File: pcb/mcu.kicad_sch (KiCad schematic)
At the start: 0 parts

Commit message: [pcb] Started STM32 schematic
Co-authored-by: Siddhant Kameswar <grimsteel@users.noreply.github.com>
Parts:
- added C1, C4, C5, C6, C7: 100nF, symbol Device:C
- added C2, C3, C8: 10uF, symbol Device:C
- added D1: D, symbol Device:D
- added J1: Conn_01x02_Pin, symbol Connector:Conn_01x02_Pin
- added R1: 1K, symbol Device:R
- added U1: STM32H750VBTx, Package_QFP:LQFP-100_14x14mm_P0.5mm, symbol MCU_ST_STM32H7:STM32H750VBTx
- added U2: W25Q64JVSSIQ_C179171, lcsc:SOIC-8_L5.3-W5.3-P1.27-LS8.0-BL, symbol lcsc:W25Q64JVSSIQ_C179171
- added U3: AMS1117-3.3, Package_TO_SOT_SMD:SOT-223-3_TabPin2, symbol Regulator_Linear:AMS1117-3.3
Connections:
- new net: R1.1, U1.6 (VBAT)
- new net: D1.2 (A), J1.1 (Pin_1)
- new net: U1.10 (VSS), U1.26 (VSS), U1.49 (VSS), U1.74 (VSS), U1.99 (VSS)
- new net +3.3V: C1.2, C3.1, C4.1, C5.1, C6.1, C7.1, C8.1, R1.2, U1.100 (VDD), U1.11 (VDD), U1.27 (VDD), U1.50 (VDD), U1.75 (VDD), U2.8 (VCC), U3.2 (VO)
- new net +BATT: C2.2, D1.1 (K), U3.3 (VI)
- new net BOOT0: U1.94 (BOOT0)
- new net FLASH_CS: U1.92 (PB6), U2.1 (~{CS})
- new net FLASH_IO_0: U1.58 (PD11), U2.5 (DI(IO0))
- new net FLASH_IO_1: U1.59 (PD12), U2.2 (DO(IO1))
- new net FLASH_IO_2: U1.1 (PE2), U2.3 (WP#(IO2))
- new net FLASH_IO_3: U1.60 (PD13), U2.7 (HOLD#orRESET#(IO3))
- new net GND: C1.1, C2.1, C3.2, C4.2, C5.2, C6.2, C7.2, C8.2, J1.2 (Pin_2), U2.4 (GND), U3.1 (GND)
- new net SPI_CLK: U1.36 (PB2), U2.6 (CLK)
- no-connect marks 0 -> 1
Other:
- note added: "Battery Connector"

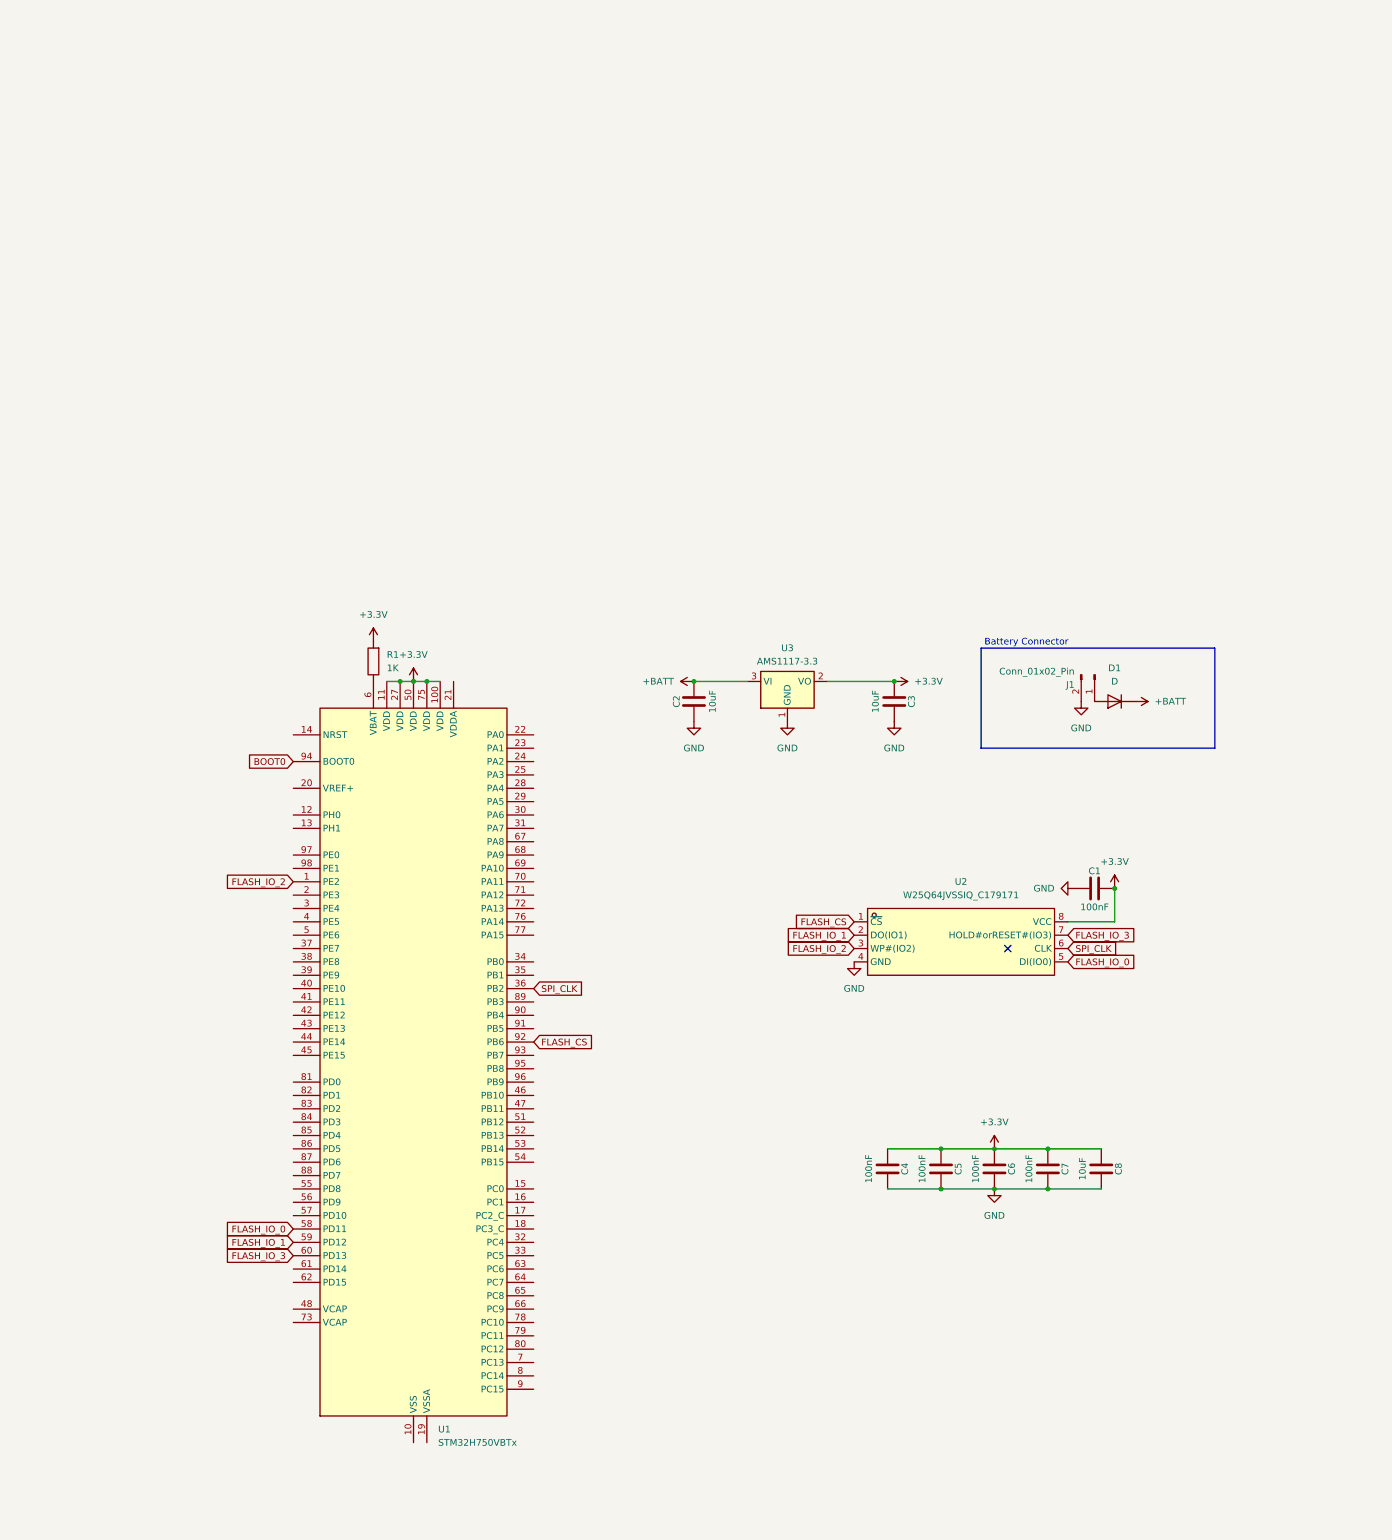
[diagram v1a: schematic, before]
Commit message: [pcb] More STM32 power
Co-authored-by: Siddhant Kameswar <grimsteel@users.noreply.github.com>
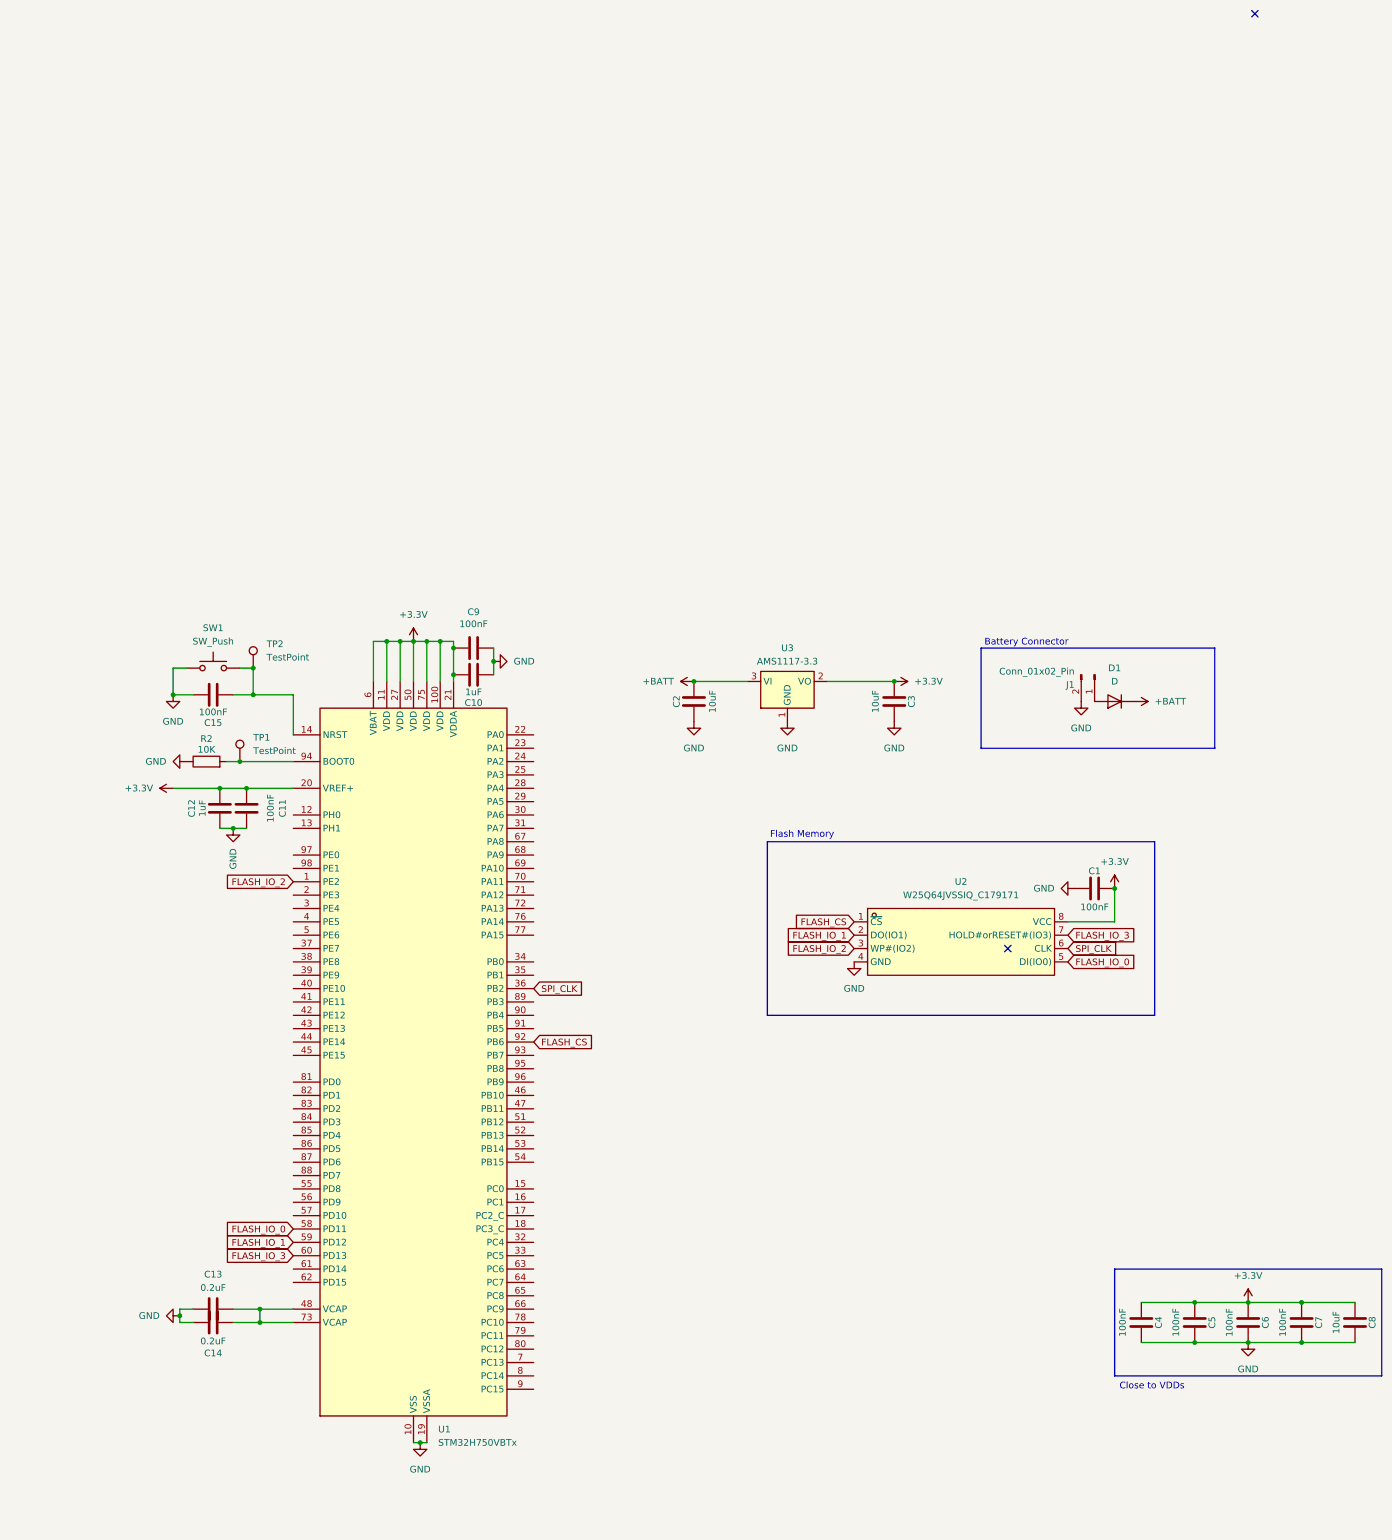
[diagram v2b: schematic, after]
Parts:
- removed R1: 1K, symbol Device:R
- added C10, C12: 1uF, symbol Device:C
- added C11, C15, C9: 100nF, symbol Device:C
- added C13, C14: 0.2uF, symbol Device:C
- added R2: 10K, symbol Device:R
- added SW1: SW_Push, symbol Switch:SW_Push
- added TP1, TP2: TestPoint, symbol Connector:TestPoint
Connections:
- net +3.3V: now also U1.20 (VREF+), U1.21 (VDDA), U1.6 (VBAT), C10.2, C11.1, C12.2, C9.1
- net GND: now also U1.10 (VSS), U1.19 (VSSA), U1.26 (VSS), U1.49 (VSS), U1.74 (VSS), U1.99 (VSS), C10.1, C11.2, C12.1, C13.1, C14.1, C15.2, C9.2, R2.1, SW1.1
- net at U1.14 (NRST): now also C15.1, SW1.2, TP2.1
- net at U1.48 (VCAP): now also U1.73 (VCAP), C13.2, C14.2
- net BOOT0: no longer names the net of U1.94 (BOOT0)
- net BOOT0: now also R2.2, TP1.1
- no-connect marks 1 -> 2
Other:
- note added: "Close to VDDs"
- note added: "Flash Memory"
- moved on the sheet: C4, C5, C6, C7, C8

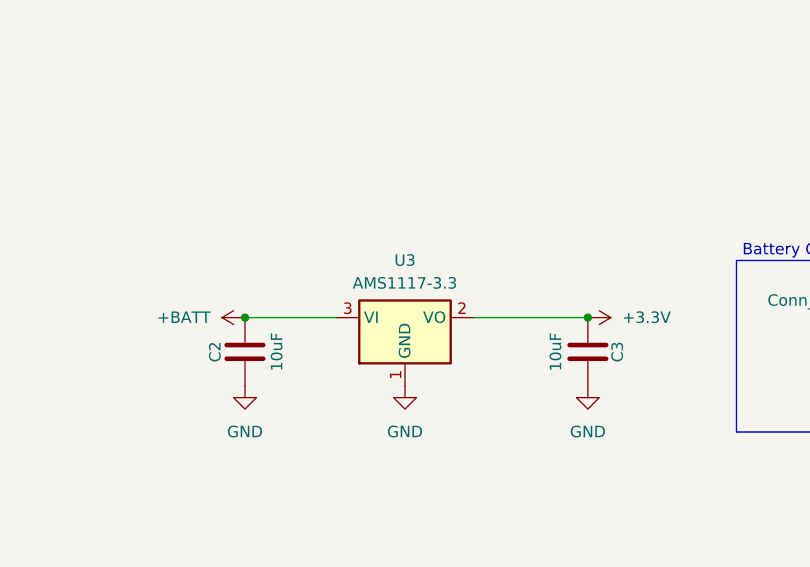
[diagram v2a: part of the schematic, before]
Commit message: [pcb] start transceiver implementation
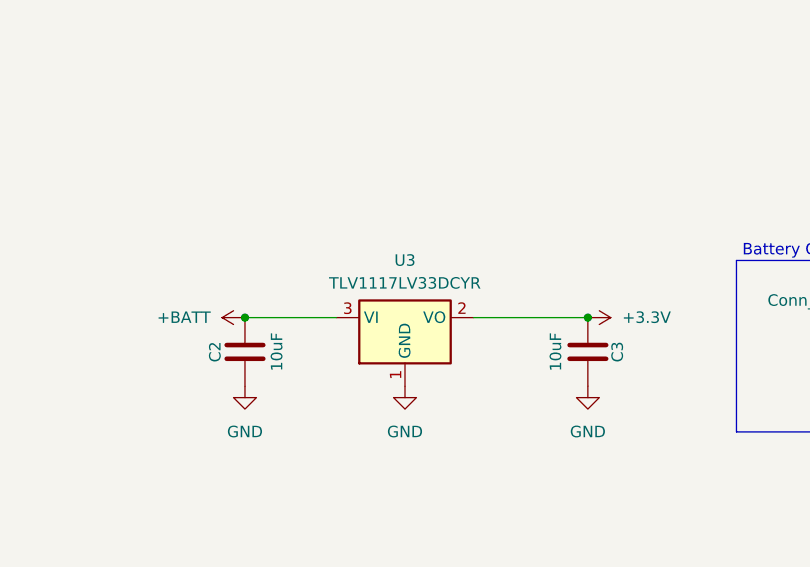
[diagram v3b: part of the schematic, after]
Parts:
- U3: value AMS1117-3.3 -> TLV1117LV33DCYR
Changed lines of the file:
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@@
 			)
 		)
-		(property "Value" "AMS1117-3.3"
+		(property "Value" "TLV1117LV33DCYR"
 			(at 162.56 22.86 0)
 			(effects
